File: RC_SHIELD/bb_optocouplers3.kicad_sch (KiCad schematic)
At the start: 41 parts, among them U1 SFH6345, U10 SFH6345, U11 SFH6345, U2 SFH6345, U9 SFH6345

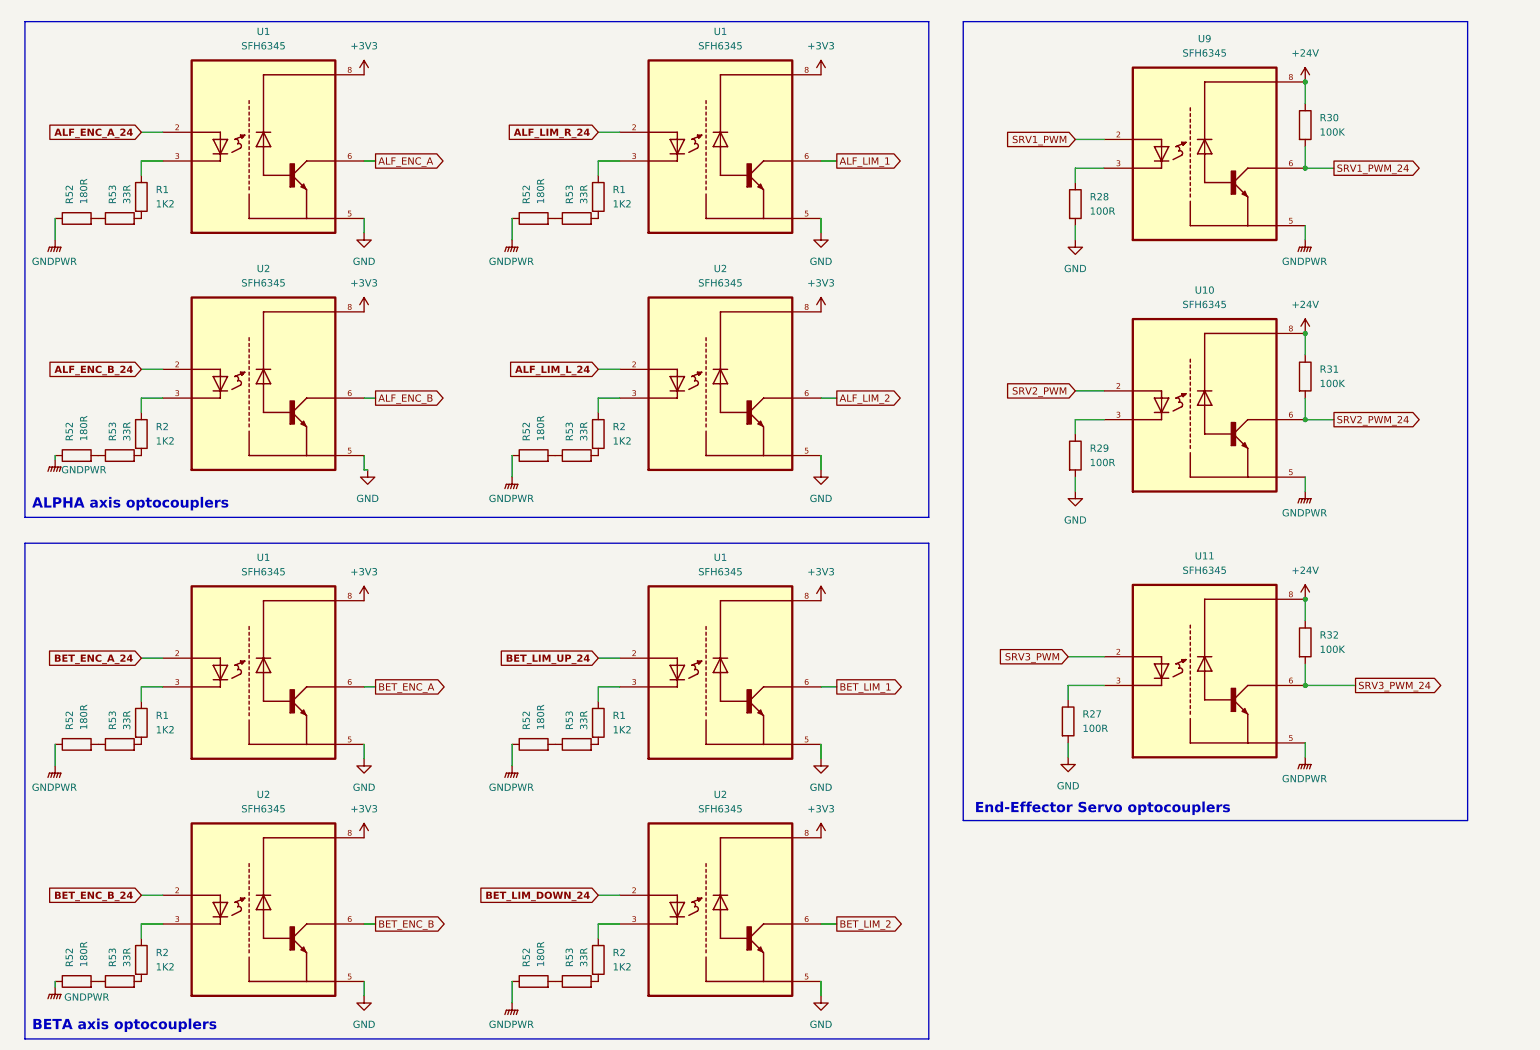
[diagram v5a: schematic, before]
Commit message: Revert "[SCH] reorganized optocouplers and tidied up page 2"
This reverts commit 005640e4067293c5014d1b79d289b32d97da3ff9.
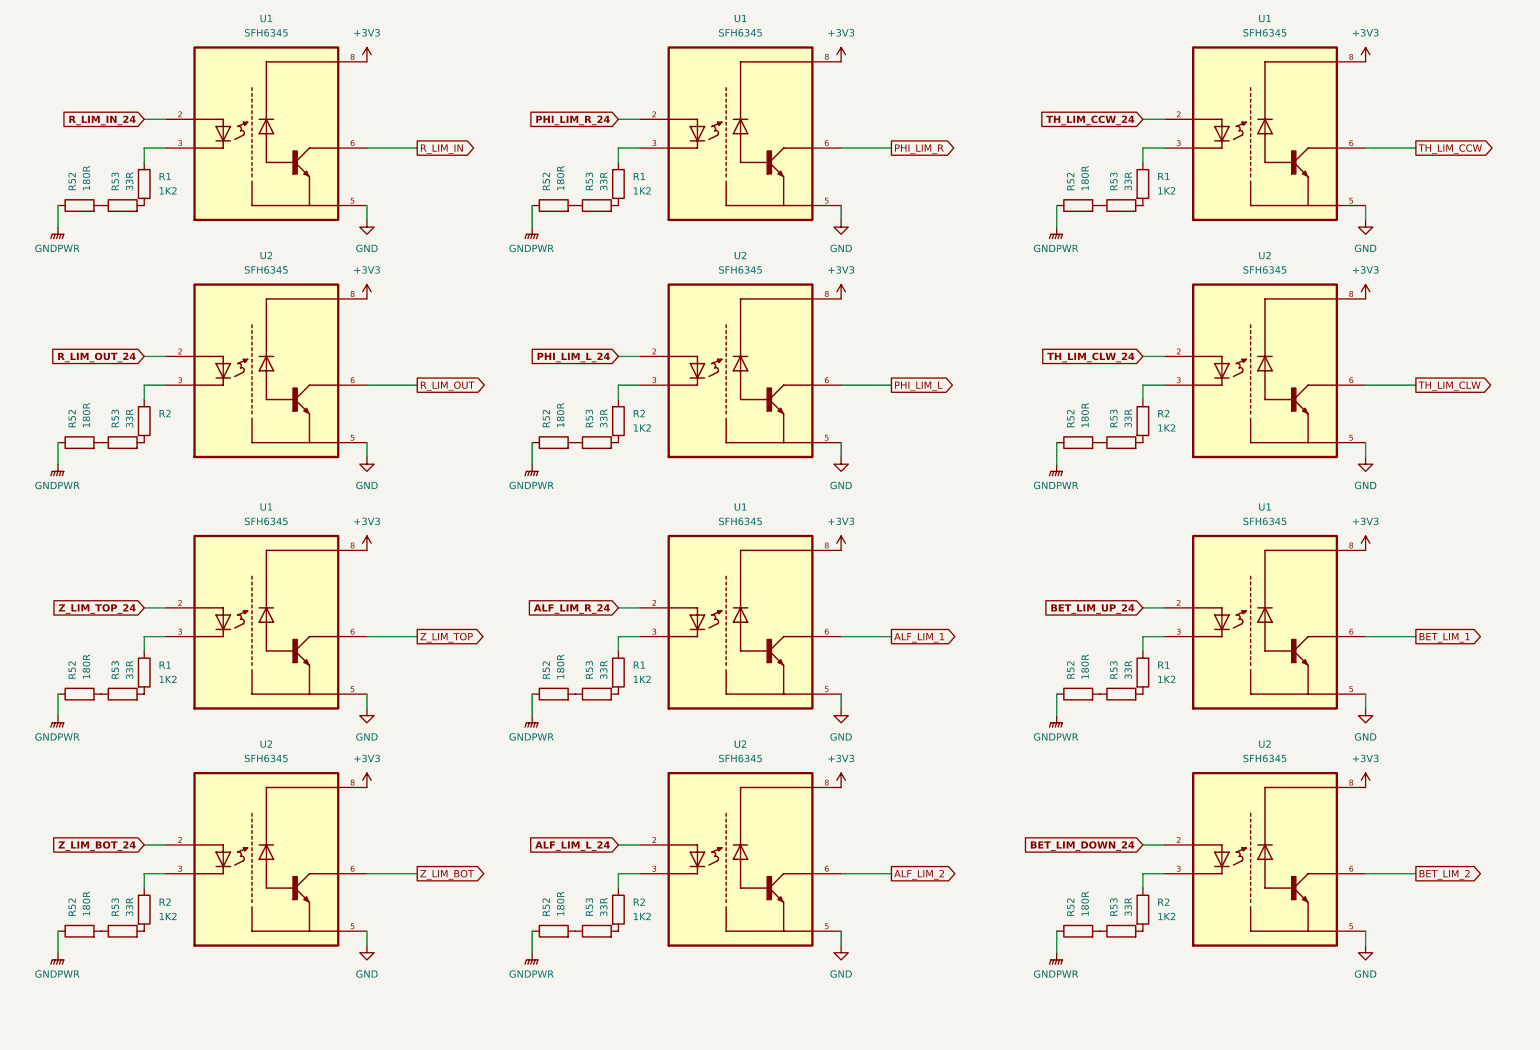
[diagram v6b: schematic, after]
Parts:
- removed R1 (x2), R2 (x2): 1K2, Resistor_SMD:R_0805_2012Metric_Pad1.20x1.40mm_HandSolder, symbol Device:R
- removed R27, R28, R29: 100R, Resistor_SMD:R_0805_2012Metric_Pad1.20x1.40mm_HandSolder, symbol Device:R
- removed R30, R31, R32: 100K, Resistor_SMD:R_0805_2012Metric_Pad1.20x1.40mm_HandSolder, symbol Device:R
- removed R52 (x4): 180R, Resistor_SMD:R_0805_2012Metric_Pad1.20x1.40mm_HandSolder, symbol Device:R
- removed R53 (x4): 33R, Resistor_SMD:R_0805_2012Metric_Pad1.20x1.40mm_HandSolder, symbol Device:R
- removed U1 (x2), U10, U11, U2 (x2), U9: SFH6345, SFH6345:DIP762W50P254L977H451Q8, symbol SFH6345:SFH6345
- added R1 (x4), R2 (x4): 1K2, Resistor_SMD:R_0805_2012Metric_Pad1.20x1.40mm_HandSolder, symbol Device:R
- added R52 (x8): 180R, Resistor_SMD:R_0805_2012Metric_Pad1.20x1.40mm_HandSolder, symbol Device:R
- added R53 (x8): 33R, Resistor_SMD:R_0805_2012Metric_Pad1.20x1.40mm_HandSolder, symbol Device:R
- added U1 (x4), U2 (x4): SFH6345, SFH6345:DIP762W50P254L977H451Q8, symbol SFH6345:SFH6345
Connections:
- net +3V3: now also U1.8, U1.8, U1.8, U1.8, U2.8, U2.8, U2.8, U2.8
- net GND: now also U1.5, U1.5, U1.5, U1.5, U2.5, U2.5, U2.5, U2.5
- net GNDPWR: now also R52.1, R52.1, R52.1, R52.1, R52.1, R52.1, R52.1, R52.1
- new net: R52.2, R53.1 (x8)
- new net: R1.2, R53.2 (x4)
- new net: R1.1, U1.3 (x4)
- new net: R2.1, U2.3 (x4)
- new net: R2.2, R53.2 (x4)
- new net PHI_LIM_L: U2.6
- new net PHI_LIM_L_24: U2.2
- new net PHI_LIM_R: U1.6
- new net PHI_LIM_R_24: U1.2
- new net R_LIM_IN: U1.6
- new net R_LIM_IN_24: U1.2
- new net R_LIM_OUT: U2.6
- new net R_LIM_OUT_24: U2.2
- new net TH_LIM_CCW: U1.6
- new net TH_LIM_CCW_24: U1.2
- new net TH_LIM_CLW: U2.6
- new net TH_LIM_CLW_24: U2.2
- new net Z_LIM_BOT: U2.6
- new net Z_LIM_BOT_24: U2.2
- new net Z_LIM_TOP: U1.6
- new net Z_LIM_TOP_24: U1.2
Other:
- note removed: "ALPHA axis optocouplers"
- note removed: "BETA axis optocouplers"
- note removed: "End-Effector Servo optocouplers"
- moved on the sheet: R1, R2, R52, R53, U1, U2

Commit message: [SCH] fixed Nucleo papercuts
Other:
- title: Karcsi (INDACT Robot Arm) - Wrist & EE optocouplers -> Karcsi (INDACT Robot Arm) - Limit switch optocouplers
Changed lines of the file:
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@@
   (paper "A4")
   (title_block
-    (title "Karcsi (INDACT Robot Arm) - Wrist & EE optocouplers")
+    (title "Karcsi (INDACT Robot Arm) - Limit switch optocouplers")
     (date "2023-10-07")
     (rev "1.1")
